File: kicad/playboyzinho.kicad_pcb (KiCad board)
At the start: 2 copper layers, 143.2 x 185.5 mm, 16 parts, among them SW1 SW_Push, SW2 SW_Push, SW3 SW_Push, SW4 SW_Push, SW5 SW_Push, SW6 SW_Push, SW7 SW_Push, SW8 SW_Push, SW9 SW_SPDT, U1 esp32-s3-pl, U7 (amplificador)_MAX98357_Module

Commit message: fix: corrige linha torta
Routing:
- net /3V3: track 49.7 -> 47.8 mm
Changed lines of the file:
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@@
 			)
 		)
+		(fp_text user ""
+			(at -11 -8 0)
+			(unlocked yes)
+			(layer "F.Fab")
+			(effects
+				(font
+					(size 1 1)
+					(thickness 0.15)
+				)
+			)
+		)
 		(fp_text user "${REFERENCE}"
 			(at 2.5 -7.5 0)
@@
 	)
 	(segment
-		(start 13.59 27.78)
-		(end 7.73 27.78)
+		(start 7.73 27.78)
+		(end 18.15 27.78)
 		(width 1)
 		(layer "B.Cu")
@@
 	)
 	(segment
-		(start 33.0385 59)
+		(start 18.15 27.78)
 		(end 33.0385 42.6685)
 		(width 1)
@@
 	)
 	(segment
-		(start 15.87 25.5)
-		(end 13.59 27.78)
-		(width 1)
-		(layer "B.Cu")
-		(net "/3V3")
-	)
-	(segment
 		(start 33.0385 42.6685)
-		(end 15.87 25.5)
+		(end 33.0385 59)
 		(width 1)
 		(layer "B.Cu")

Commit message: refact: tira sd do amplificador do GPIO11 e coloca num SPDT
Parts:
- added SW10: SW_SPDT, lib-do-playboy:alavanca, F.Cu at (111.3, 167.2)
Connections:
- U1 pad 17: /AMP_SD -> unconnected-(U1-GPIO11-Pad17)
- U1 pad 27: unconnected-(U1-GPIO2-Pad27) -> /Button-1
- U1 pad 28: /Button-1 -> /Button-2
- U1 pad 29: /Button-2 -> /Button-3
- U1 pad 30: /Button-3 -> /Button-5
- U1 pad 31: /Button-5 -> /Button-4
- U1 pad 32: /Button-4 -> /Button-6
- U1 pad 38: /Button-6 -> unconnected-(U1-GPIO48-Pad38)
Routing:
- net /AMP_SD: track 28.5 -> 236.1 mm
- net /3V3: track 47.8 -> 221.2 mm
- net /Button-6: track 41.5 -> 26.7 mm
- net Net-(SW9-B): track 107.2 -> 110.7 mm
- net /Button-5: track 49.0 -> 46.3 mm
- net /Button-3: track 93.1 -> 90.3 mm
- net /Button-2: track 79.3 -> 76.5 mm
- net /Button-1: track 84.5 -> 81.7 mm
- net Net-(SW9-C): track 279.2 -> 281.7 mm
- net /Button-4: track 81.2 -> 78.9 mm

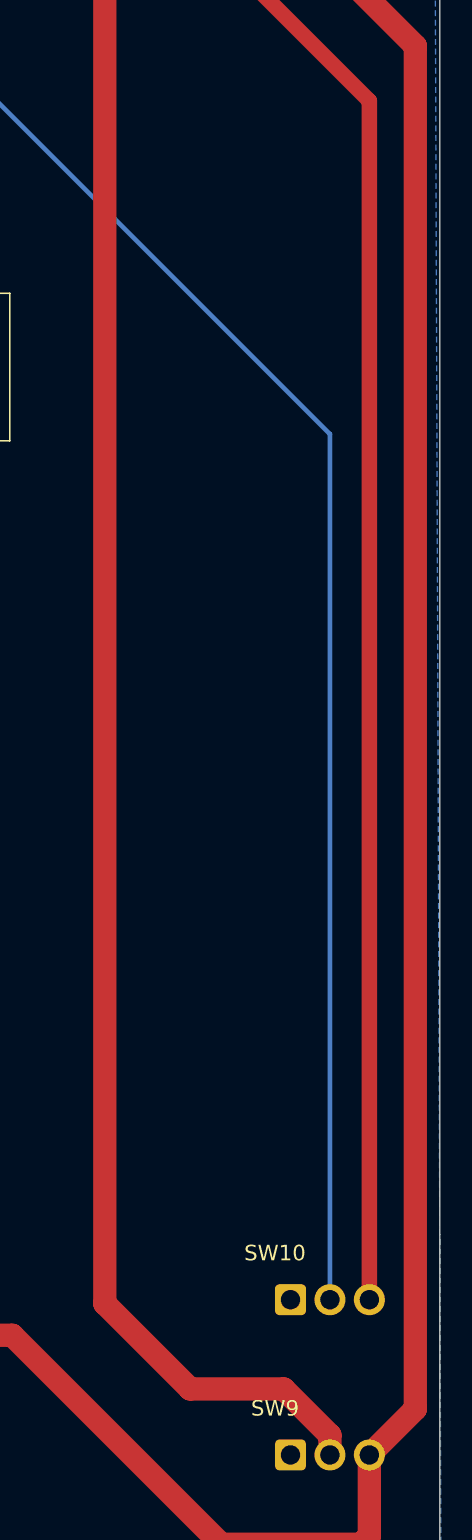
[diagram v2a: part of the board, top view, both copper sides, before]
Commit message: feat: atualiza relatório e arquivo de conexões
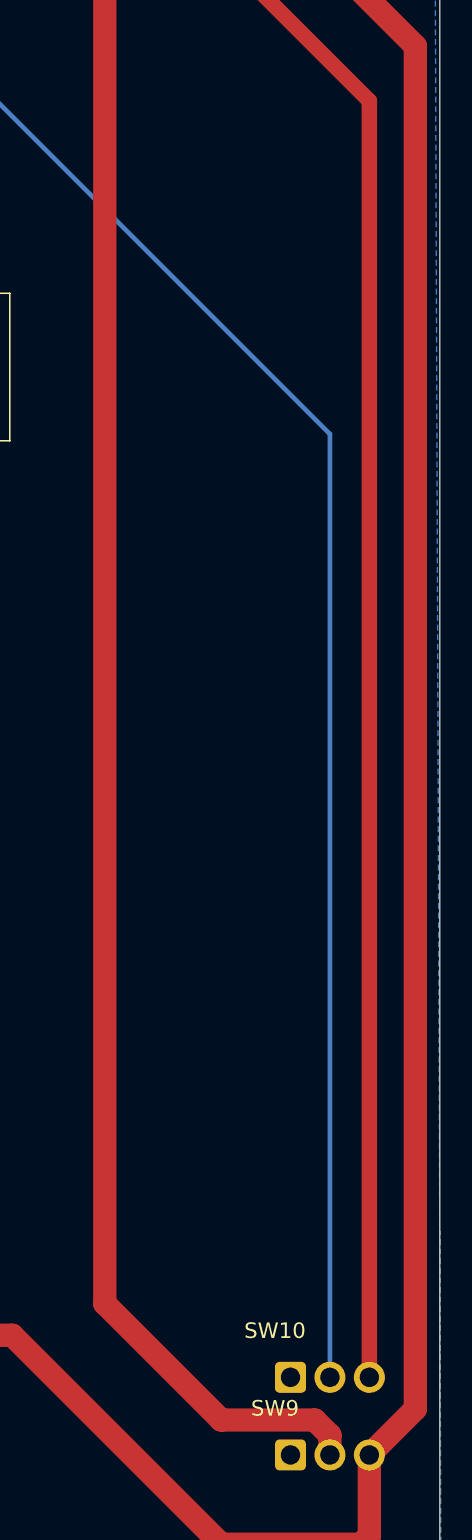
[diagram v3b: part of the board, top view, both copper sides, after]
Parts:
- moved SW10 5.00 mm to (111.3, 172.2)
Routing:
- net /AMP_SD: track 236.1 -> 241.1 mm
- net /3V3: track 221.2 -> 226.2 mm
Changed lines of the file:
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@@
 	(footprint "lib-do-playboy:alavanca"
 		(layer "F.Cu")
-		(at 111.33 167.25)
+		(at 111.33 172.25)
 		(property "Reference" "SW10"
 			(at -1 -3 0)
@@
 	)
 	(segment
-		(start 9.37 7)
-		(end 113.87 111.5)
+		(start 113.87 111.5)
+		(end 113.87 172.25)
 		(width 0.3)
 		(layer "B.Cu")
@@
 	)
 	(segment
-		(start -7.59 20.46)
-		(end 5.87 7)
+		(start 9.37 7)
+		(end 113.87 111.5)
 		(width 0.3)
 		(layer "B.Cu")
@@
 	)
 	(segment
-		(start 113.87 111.5)
-		(end 113.87 167.25)
+		(start -7.59 20.46)
+		(end 5.87 7)
 		(width 0.3)
 		(layer "B.Cu")
@@
 	)
 	(segment
-		(start 98.87 72.5)
-		(end 116.41 90.04)
-		(width 1)
-		(layer "F.Cu")
-		(net "/3V3")
-	)
-	(segment
-		(start 62.87 59)
-		(end 72.87 69)
+		(start 116.41 90.04)
+		(end 116.41 172.25)
 		(width 1)
 		(layer "F.Cu")
@@
 	)
 	(segment
-		(start 116.41 90.04)
-		(end 116.41 167.25)
+		(start 62.87 59)
+		(end 72.87 69)
 		(width 1)
 		(layer "F.Cu")
@@
 	)
 	(segment
-		(start 86.87 69)
-		(end 90.37 72.5)
+		(start 98.87 72.5)
+		(end 116.41 90.04)
 		(width 1)
 		(layer "F.Cu")
@@
 	)
 	(segment
+		(start 86.87 69)
+		(end 90.37 72.5)
+		(width 1)
+		(layer "F.Cu")
+		(net "/3V3")
+	)
+	(segment
 		(start 7.73 27.78)
 		(end 18.15 27.78)
@@
 	)
 	(segment
-		(start 104.87 173)
-		(end 99.37 167.5)
+		(start 112.892792 175)
+		(end 106.87 175)
 		(width 1.5)
 		(layer "F.Cu")
@@
 	)
 	(segment
-		(start 99.37 79.3315)
-		(end 97.0385 77)
+		(start 113.87 175.977208)
+		(end 112.892792 175)
 		(width 1.5)
 		(layer "F.Cu")
@@
 	)
 	(segment
-		(start 113.87 175.977208)
-		(end 110.892792 173)
+		(start 113.87 177.25)
+		(end 113.87 175.977208)
 		(width 1.5)
 		(layer "F.Cu")
@@
 	)
 	(segment
-		(start 113.87 177.25)
-		(end 113.87 175.977208)
+		(start 106.87 175)
+		(end 99.37 167.5)
 		(width 1.5)
 		(layer "F.Cu")
@@
 	)
 	(segment
-		(start 110.892792 173)
-		(end 104.87 173)
+		(start 99.37 79.3315)
+		(end 97.0385 77)
 		(width 1.5)
 		(layer "F.Cu")
